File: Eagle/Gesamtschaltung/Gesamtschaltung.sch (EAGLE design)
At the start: 105 parts, among them IC02 LM1117-5.0, IC04 24LC256, IC06 LM1117-5.0, IC1 MC9S08AW60, Q1 4M9152, X4 SPP

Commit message: exp Dokumentation, 9 pages now
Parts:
- removed C11, C12: 1µF, deto:C1
- removed C13, C14, C18, C19, C21, C22: 10nF, deto:C1
- removed D2: SA5.0CA, diode:DIODE-SMB
- removed D3: 1N4007, deto:DHCMELF
- removed IC04: 24LC256, microchip:24CLC256SM
- removed IC06: LM1117-5.0, deto:LM1117DT
- removed JP10, JP11, JP12, JP13, JP7, JP8, JP9: (no value), pinhead:PINHD-1X3
- removed R33, R34, R40, R50, R51, R52, R53, R55, R56, R57, R58, R59, R60, R61, R62, R63, R64, R65, R66, R85, R86, R87, R88: 10k, deto:R1
- removed R47: 680R, deto:R1
- removed R67, R68, R69, R70, R71, R72, R73, R74: 100R, deto:R1
- removed X3, X8: (no value), CONNECT:KLEMME2
- removed X4: SPP, CONNECT:SPP
- removed X6, X7, X9: (no value), CONNECT:KLEMME4
- added IC03: LP2950CDT-3.3, v-reg:LP2950CDT-3.3
- added LED1, LED2: (no value), led:LED3MM
- added Q2: P5N50, transistor-fet:BUZ11
- added R10, R11, R12, R14, R15, R16, R17, R18, R19, R20, R21, R22, R27, R28, R29, R7, R8: (no value), rcl:R-EU_M0805
- added T10, T11, T12, T13, T14: (no value), deto:TASTERTHT
- C6: value 10nF -> 1µF
- C7: value 10nF -> 100nF
- D1: value SA5.0CA -> 1N4004; device diode:DIODE-SMB -> diode:1N4004
- JP2, JP4: device pinhead:PINHD-1X3 -> pinhead:PINHD-1X2
- JP5: device pinhead:PINHD-1X3 -> pinhead:PINHD-1X8
- JP6: device pinhead:PINHD-1X3 -> pinhead:PINHD-1X4
- R2, R23, R24, R25, R26, R3, R30: value 10k -> (none); device deto:R1 -> rcl:R-EU_M0805
- R31, R32: value 10k -> (none); device deto:R1 -> rcl:R-EU_R0805
- R4, R5: value 27R -> (none); device deto:R1 -> rcl:R-EU_M0805
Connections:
- removed net ADCPB0: C22.2, IC1PORTB.PB0, R30.1
- removed net ADCPB1: C21.2, IC1PORTB.PB1, R31.1
- removed net ADCPB2: C19.2, IC1PORTB.PB2, R32.1
- removed net ADCPB3: C18.2, IC1PORTB.PB3, R33.1
- removed net ADCPB4: C14.2, IC1PORTB.PB4, R34.1
- removed net ADCPB5: C13.2, IC1PORTB.PB5, R40.1
- removed net ADCPB6: C6.2, IC1PORTB.PB6, R2.1
- removed net ADCPB7: C7.2, IC1PORTB.PB7, R3.1
- removed net ANA0: R30.2
- removed net ANA1: R31.2
- removed net ANA2: R32.2
- removed net ANA3: R33.2
- removed net ANA4: JP5.2, R34.2, X9.1
- removed net ANA5: JP4.2, R40.2, X9.2
- removed net ANA6: JP3.2, R2.2, X9.3
- removed net ANA7: JP2.2, R3.2, X9.4
- removed net N$100: JP3.1, R86.2
- removed net N$101: JP4.1, R87.2
- removed net N$102: JP5.1, R88.2
- removed net N$40: JP8.3, R52.1
- removed net N$41: JP7.3, R51.1
- removed net N$53: R4.1, X3.1
- removed net N$54: R67.2, T1.B2
- removed net N$56: R68.2, T2.B2
- removed net N$57: JP6.3, R50.1
- removed net N$59: R70.2, T4.B2
- removed net N$61: JP6.1, R59.2
- removed net N$62: JP7.1, R60.2
- removed net N$63: JP8.1, R61.2
- removed net N$64: JP9.1, R62.2
- removed net N$65: R74.2, T8.B2
- removed net N$66: JP10.1, R63.2
- removed net N$67: JP11.1, R64.2
- removed net N$68: JP12.1, R65.2
- removed net N$69: JP13.1, R66.2
- removed net N$70: C11.2, D3.K, IC06.VI
- removed net N$71: D3.A, X4.2
- removed net N$72: JP12.2
- removed net N$73: JP10.2
- removed net N$74: JP6.2
- removed net N$75: JP11.2
- removed net N$76: JP9.2
- removed net N$77: JP8.2
- removed net N$78: JP7.2
- removed net N$89: JP5.3, R26.1
- removed net N$96: JP4.3, R25.1
- removed net N$97: JP3.3, R24.1
- removed net N$98: JP2.3, R23.1
- removed net N$99: JP2.1, R85.2
- removed net PF0: R67.1, X6.1
- removed net PF1: R68.1, X6.2
- removed net PF2: R69.1, X6.3
- removed net PF3: R70.1, X6.4
- removed net PF4: R71.1, X7.1
- removed net PF5: R72.1, X7.2
- removed net PF6: R73.1, X7.3
- removed net PF7: R74.1, X7.4
- removed net RX2: IC1PORTC.PC5
- removed net SCL: IC04.SCL, IC1PORTC.PC0
- removed net SDA: IC04.SDA, IC1PORTC.PC1, R47.1
- removed net TX2: IC1PORTC.PC3
- new net +12V: D1.C, D4.A, JP2.2, JP4.1
- new net +3V3: C6.2, IC03.OUT, JP5.1
- new net N$14: IC1PORTF.PF1, R2.1
- new net N$2: R20.2, R3.2, T1.B2
- new net N$21: IC1PORTF.PF3, R5.1
- new net N$23: IC1PORTF.PF4, R7.1
- new net N$24: IC1PORTF.PF5, R8.1
- new net N$25: IC1PORTF.PF6, R10.1
- new net N$26: IC1PORTF.PF7, R11.1
- new net N$27: IC1PORTF.PF0, R3.1
- new net N$28: R24.2, R29.1, T13.B2
- new net N$29: IC1PORTD.PD5, R31.1
- new net N$3: R19.2, R2.2, T2.B2
- new net N$30: R23.2, R28.1, T12.B2
- new net N$31: R25.2, R30.1, T14.B2
- new net N$32: C7.1, D1.A, JP4.2, Q2.D
- new net N$33: LED2.A, R32.2
- new net N$42: IC1PORTE.PE0, JP6.1
- new net N$44: IC1PORTE.PE2, JP6.3
- new net N$45: IC1PORTE.PE3, JP6.4
- new net N$5: R18.2, R4.2, T3.B2
- new net N$6: R17.2, R5.2, T4.B2
- new net N$7: R16.2, R7.2, T5.B2
- net +5V: now also IC03.IN, JP3.2, T10.A1, T11.A1, T12.A1, T13.A1; no longer C12.2, D1.C, D2.C, IC04.VCC, IC06.VO, R23.2, R24.2, R25.2, R26.2, R4.2, R47.2, R5.2
- net GND: now also C7.2, IC03.GND, JP2.1, JP3.3, JP5.3, LED1.C, LED2.C, Q2.S, R12.1, R14.1, R15.1, R16.1, R17.1, R18.1, R19.1, R20.1, R26.2, R27.2, R28.2, R29.2, R30.2; no longer C11.1, C12.1, C13.1, C14.1, C18.1, C19.1, C21.1, C22.1, C7.1, D1.A, D2.A, IC04.A0, IC04.A1, IC04.A2, IC04.GND, IC04.WP, IC06.GND, R59.1, R60.1, R61.1, R62.1, R63.1, R64.1, R65.1, R66.1, R85.1, R86.1, R87.1, R88.1, X3.2, X4.1, X4.3, X8.2
- net N$10: now also R21.2, R26.1, T10.B2; no longer IC1PORTD.PD3
- net N$11: now also R15.2, R8.2, T6.B2; no longer JP13.3, R58.1
- net N$12: now also R10.2, R14.2, T7.B2; no longer JP12.3, R57.1
- net N$13: now also R11.2, R12.2, T8.B2; no longer R69.2, T3.B2
- net N$15: now also IC1PORTF.PF2, R4.1; no longer JP13.2
- net N$17: now also IC1PORTD.PD1, R22.1; no longer IC1PORTD.PD4
- net N$18: now also IC1PORTD.PD3, R24.1; no longer IC1PORTD.PD5
- net N$19: now also R22.2, R27.1, T11.B2; no longer IC1PORTD.PD6
- net N$20: now also IC1PORTD.PD6, R32.1; no longer IC1PORTD.PD7
- net N$34: now also LED1.A, R31.2; no longer JP11.3, R56.1
- net N$35: now also IC1PORTE.PE7, JP5.7; no longer R71.2, T5.B2
- net N$36: now also IC1PORTB.PB0, Q2.G; no longer R72.2, T6.B2
- net N$37: now also IC1PORTB.PB1, JP3.1; no longer R73.2, T7.B2
- net N$38: now also IC1PORTE.PE6, JP5.5; no longer JP10.3, R55.1
- net N$39: now also IC1PORTE.PE5, JP5.4; no longer JP9.3, R53.1
- net N$4: now also R21.1
- net N$43: now also IC1PORTE.PE1, JP6.2; no longer R5.1, X8.1
- net N$8: now also IC1PORTD.PD2, R23.1; no longer IC1PORTD.PD1
- net N$9: now also IC1PORTD.PD4, R25.1; no longer IC1PORTD.PD2
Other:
- note added: "Alarmanlage"
- note added: "Audio & PIR"
- note added: "BDM-Modul"
- note added: "LCD/Quartz"
- note added: "Maturaprojekt"
- note added: "RFID-RC522"
- note added: "Tastenfeld"
- note added: "Versorgung"
- note removed: "Analoge Eingänge"
- note removed: "Digital Input, BDM-Connector"
- note removed: "Extern ADC Input"
- note removed: "LC-Display"
- note removed: "Pull-Down Select"
- note removed: "Pull-Up or"
- note removed: "zu RS232"

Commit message: add Board
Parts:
- removed IC02: LM1117-5.0, deto:LM1117DT
- added IC04: (no value), v-reg:78XXS
- added R33: 1k, rcl:R-EU_0207/10
- added R34, R35, R36, R37, R38, R40, R41, R42: 1k, rcl:R-EU_M0805
- C6, C8, C9: value 1µF -> 100n
- D4: device deto:DHCMELF -> deto:DHC
- R10, R11, R2, R21, R22, R23, R24, R25, R3, R31, R32, R4, R5, R7, R8: value (none) -> 1k
- R12, R14, R15, R16, R17, R18, R19, R20, R26, R27, R28, R29, R30: value (none) -> 10k
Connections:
- new net N$32: IC1PORTE.PE0, R34.1
- new net N$40: Q2.G, R33.1
- new net N$41: IC1PORTB.PB1, R35.2
- new net N$47: IC1PORTE.PE5, R40.1
- new net N$48: IC1PORTE.PE6, R41.1
- new net N$53: IC1PORTE.PE7, R42.1
- new net N$54: JP6.3, R37.2
- new net N$56: JP6.2, R36.2
- new net N$57: JP6.1, R34.2
- net +5V: now also IC04.OUT, T14.A1; no longer IC02.VO
- net GND: now also IC04.GND; no longer IC02.GND
- net N$1: now also IC04.IN; no longer IC02.VI
- net N$20: now also IC1PORTD.PD7; no longer IC1PORTD.PD6
- net N$29: now also IC1PORTD.PD6; no longer IC1PORTD.PD5
- net N$35: now also R42.2; no longer IC1PORTE.PE7
- net N$36: now also R33.2; no longer Q2.G
- net N$37: now also R35.1; no longer IC1PORTB.PB1
- net N$38: now also R41.2; no longer IC1PORTE.PE6
- net N$39: now also R40.2; no longer IC1PORTE.PE5
- net N$42: now also IC1PORTE.PE1, R36.1; no longer IC1PORTE.PE0, JP6.1
- net N$43: now also IC1PORTE.PE2, R37.1; no longer IC1PORTE.PE1, JP6.2
- net N$44: now also IC1PORTE.PE3, R38.1; no longer IC1PORTE.PE2, JP6.3
- net N$45: now also R38.2; no longer IC1PORTE.PE3
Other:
- note removed: "BDM-Module"
- moved on the sheet: C7, D1, IC1PORTB, IC1PORTD, IC1PORTE, IC1PORTF, JP3, JP4, JP5, JP6, Q2, R31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

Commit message: edit Dokumentation, add diverse Bilder
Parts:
- LED1: value (none) -> RED
- LED2: value (none) -> GREEN

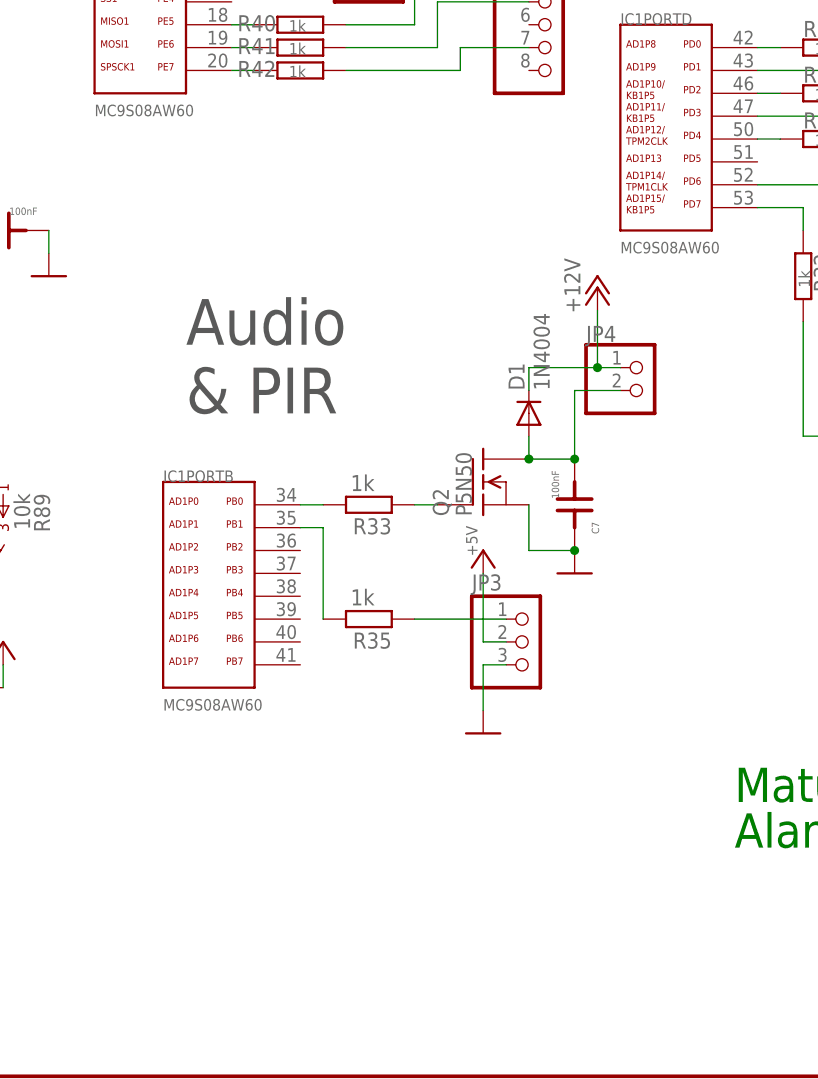
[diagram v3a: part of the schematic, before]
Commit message: add bilder Schaltung, add Bauteilliste, add Bild MosFet, extend Dokumentation
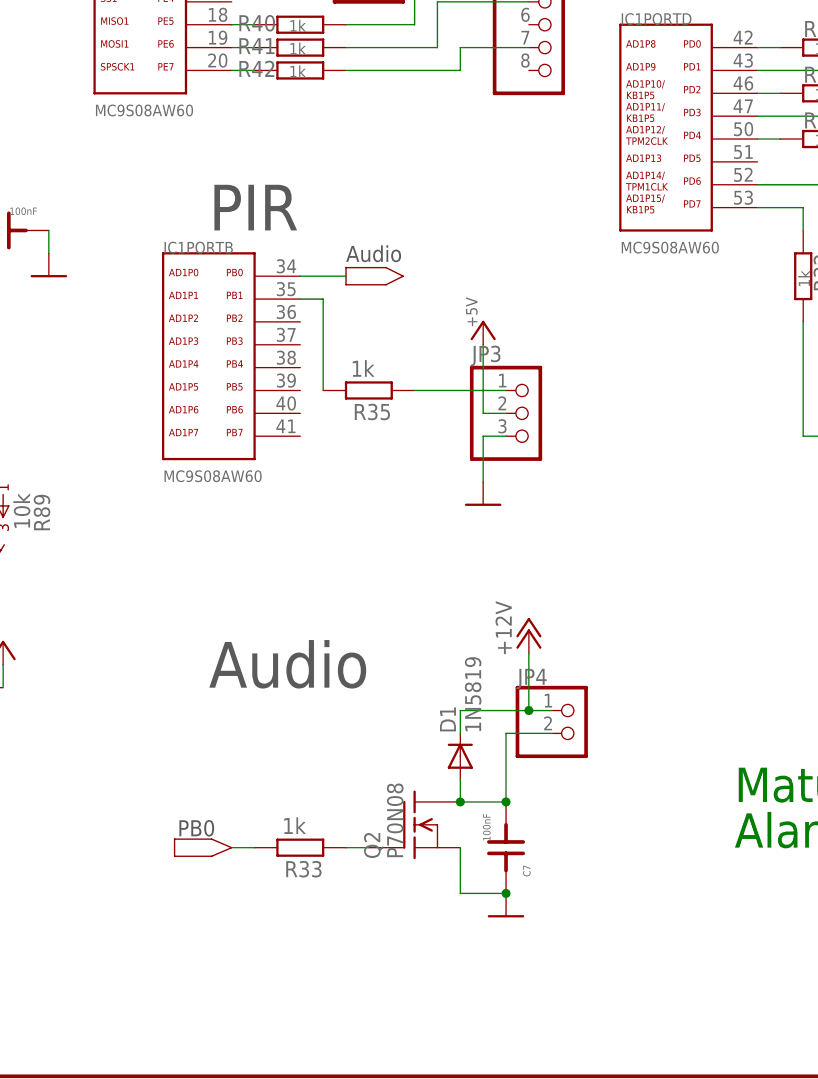
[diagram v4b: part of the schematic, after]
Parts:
- D1: value 1N4004 -> 1N5819
- Q2: value P5N50 -> P70N08
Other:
- note added: "Audio"
- note added: "PB0"
- note added: "PIR"
- note removed: "Audio & PIR"
- moved on the sheet: C7, D1, IC1PORTB, JP3, JP4, Q2, R33, R35
